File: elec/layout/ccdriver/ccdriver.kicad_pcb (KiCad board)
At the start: 2 copper layers, 40 x 40 mm, 0 parts

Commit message: readme
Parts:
- added C1: 25V 1uF X5R ±10% 0402 Multilayer Ceramic Capacitors MLCC - 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, lib:C0402, F.Cu at (172.7, 118.1)
- added C2: 25V 1uF X5R ±10% 0402 Multilayer Ceramic Capacitors MLCC - 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, lib:C0402, F.Cu at (169.2, 118.1)
- added C3: 16V 4.7uF X5R ±10% 0603 Multilayer Ceramic Capacitors MLCC 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, lib:C0603, F.Cu at (177.4, 117.1)
- added C4: 50V 1uF X5R ±10% 0603 Multilayer Ceramic Capacitors MLCC - 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, lib:C0603, F.Cu at (177.4, 112.6)
- added R1: 62.5mW Thick Film Resistors 50V ±100ppm/℃ ±1% 576Ω 0402 Chi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, lib:R0402, F.Cu at (169.2, 120.0)
- added R2: 62.5mW Thick Film Resistors 50V ±100ppm/℃ ±1% 4.7kΩ 0402 Ch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, lib:R0402, F.Cu at (215.3, 104.7)
- added R3: 62.5mW Thick Film Resistors 50V ±100ppm/℃ ±1% 4.7kΩ 0402 Ch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, lib:R0402, F.Cu at (218.3, 104.6)
- added R4: 62.5mW Thick Film Resistors 50V ±1% 300mΩ 0402 Chip Resisto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, lib:R0402, F.Cu at (182.9, 112.3)
- added U1: ?, lib:WSON-10_L2.0-W2.0-P0.40-BL-EP, F.Cu at (171.0, 118.8)
- added U2: ?, lib:SC-70-5_L2.1-W1.3-P0.65-LS2.1-BR, F.Cu at (182.9, 115.8)
- added U3: ?, lib:USB-C-SMD_KH-TYPE-C-16P, F.Cu at (216.5, 109.2)
- added U4: ?, lib:IND-SMD_L4.5-W4.0, F.Cu at (185.8, 103.3)
- added U5: ?, lib:SOD-923_L0.8-W0.6-LS1.0-RD-1, F.Cu at (176.6, 121.3)
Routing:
- net bms.ic-vcc: track 0.00 -> 6.47 mm, vias 0 -> 2
- net gnd: track 0.00 -> 4.50 mm
- net iset: track 0.00 -> 2.76 mm
- net cc2: track 0.00 -> 1.65 mm
- net cc1: track 0.00 -> 1.60 mm
- net vcc-1: track 0.00 -> 1.16 mm
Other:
- board outline removed

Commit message: edited cc driver
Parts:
- moved U3 45.0 mm to (173.1, 121.0), turned to -90 degrees
- moved R3 44.5 mm to (177.6, 122.8), turned to 0 degrees
- moved R2 40.6 mm to (177.6, 119.8), turned to 0 degrees
- moved L1 17.2 mm to (182.9, 120.3)
- moved R1 13.1 mm to (180.2, 112.7), turned to -90 degrees
- moved C4 11.7 mm to (187.0, 119.2), turned to -90 degrees
- moved C2 11.5 mm to (180.2, 114.6), turned to 90 degrees
- moved D1 10.4 mm to (186.0, 117.0), turned to 180 degrees
- moved U1 8.95 mm to (178.4, 113.9), turned to 180 degrees
- moved C1 5.34 mm to (176.7, 114.6), turned to 90 degrees
- moved R4 2.72 mm to (185.0, 114.0)
- moved C3 2.16 mm to (179.5, 116.5), turned to 180 degrees
- renumbered U5 to D1, U4 to L1
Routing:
- net bms.ic-vcc: track 6.47 -> 17.7 mm
- net sw: track 0.00 -> 5.02 mm
- net vcc-1: track 1.16 -> 4.17 mm
- net vcc: track 0.00 -> 1.65 mm
- net fb: track 0.00 -> 1.40 mm

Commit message: ccdriver
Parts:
- added C1: 25V 100nF X5R ±10% 0201 Multilayer Ceramic Capacitors MLCC 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, lib:C0201, F.Cu at (188.8, 116.5)
- added C6: 25V 10uF X5R ±10% 0805 Multilayer Ceramic Capacitors MLCC -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, lib:C0805, F.Cu at (172.4, 114.2)
- added R1: 50mW Thick Film Resistors ±5% 510Ω 0201 Chip Resistor - Sur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, lib:R0201, F.Cu at (191.0, 113.5)
- added U1: ?, lib:QFN-20_L3.0-W3.0-P0.40-TL-EP1.7, F.Cu at (191.8, 116.2)
- added U5: ?, lib:KEY-SMD_4P-L4.2-W3.2-P2.20-LS4.6, F.Cu at (191.8, 121.0)
- moved R4 0.60 mm to (178.0, 122.3)
- moved U4 0.60 mm to (173.5, 120.6)
- moved R3 0.60 mm to (178.0, 119.3)
- moved C4 0.25 mm to (179.5, 116.8)
- renumbered C1 to C2, C2 to C3, C3 to C4, C4 to C5, R1 to R2, R2 to R3, R3 to R4, R4 to R5, U1 to U2, U2 to U3, U3 to U4
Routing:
- net vcc-1: track 4.17 -> 13.4 mm, vias 0 -> 1
- net uc.ic-gnd: track 0.00 -> 6.97 mm, vias 0 -> 1
- net vcc: track 1.65 -> 8.25 mm, vias 0 -> 1
- net uc.ic-vcc: track 0.00 -> 4.26 mm
- net bms.ic-vcc: track 17.7 -> 19.3 mm
- net pa0_reset_updi: track 0.00 -> 1.21 mm, vias 0 -> 1
- net updi: track 0.00 -> 1.17 mm
- net nc: vias 0 -> 2
- net gnd: vias 0 -> 5
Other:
- board text added: "gnd"
- board text added: "updi"
- board text added: "vcc"

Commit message: ccdriver updates
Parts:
- added C7: 16V 4.7uF X5R ±10% 0603 Multilayer Ceramic Capacitors MLCC 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, lib:C0603, F.Cu at (187.8, 120.5)
- added CHG: ?, lib:LED0603-RD, F.Cu at (192.5, 122.8)
- added FULL: ?, lib:LED0603-RD, F.Cu at (192.5, 121.0)
- added R5: 62.5mW Thick Film Resistors 50V ±100ppm/℃ ±1% 220Ω 0402 Chi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, lib:R0402, F.Cu at (190.0, 121.0)
- added R6: 62.5mW Thick Film Resistors 50V ±1% ±200ppm/℃ 100Ω 0402 Chi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, lib:R0402, F.Cu at (189.8, 122.8)
- moved U5 20.1 mm to (173.2, 113.4)
- moved C6 11.8 mm to (178.8, 124.2), turned to 0 degrees
- moved C5 0.91 mm to (187.8, 118.8), turned to 0 degrees
- moved R3 0.26 mm to (178.0, 119.6)
- renumbered R5 to R7
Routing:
- net bms.ic-vcc: track 19.3 -> 21.6 mm
- net charge_led.resistor-cathode: track 0.00 -> 1.91 mm
- net full_led.resistor-cathode: track 0.00 -> 1.46 mm
- net gnd: track 4.50 -> 5.43 mm
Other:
- board outline added: 25.2 x 14.8 mm

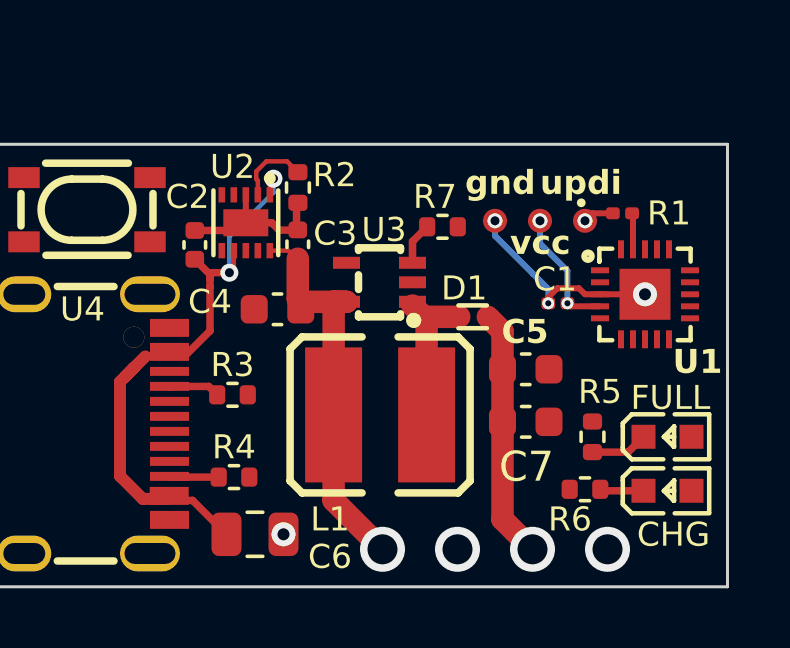
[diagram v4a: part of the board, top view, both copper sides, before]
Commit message: added 3v reg + layout edits
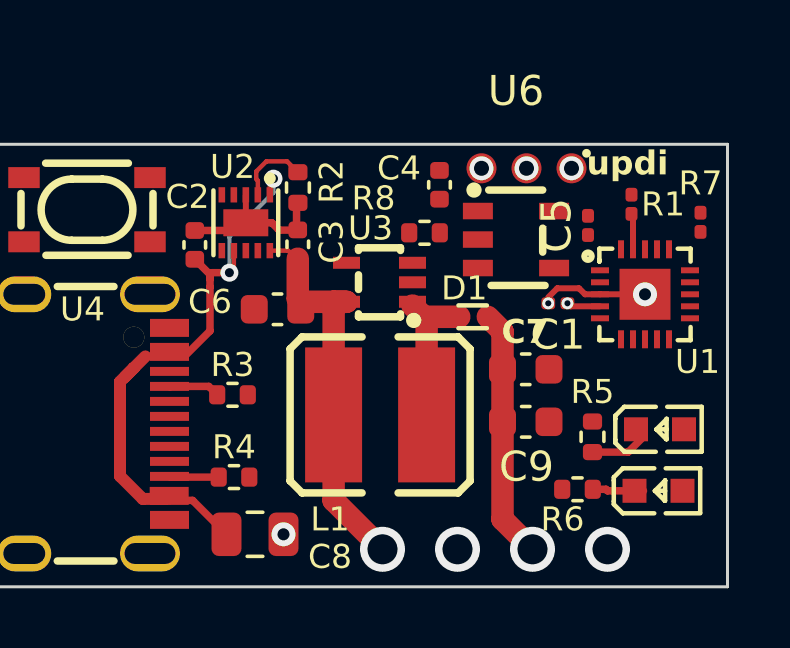
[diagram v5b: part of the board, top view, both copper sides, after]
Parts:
- added C4: 25V 1uF X5R ±10% 0402 Multilayer Ceramic Capacitors MLCC - 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, lib:C0402, F.Cu at (184.9, 112.6)
- added C5: 10V 1uF X5R ±20% 0201 Multilayer Ceramic Capacitors MLCC - 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, lib:C0201, F.Cu at (189.8, 114.0)
- added R7: 50mW Thick Film Resistors 25V ±1% ±200ppm/℃ 510kΩ 0201 Chip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, lib:R0201, F.Cu at (193.6, 113.8)
- added U6: ?, lib:SOT-23-5_L3.0-W1.7-P0.95-LS2.8-TL, F.Cu at (187.4, 114.4)
- moved R8 0.63 mm to (184.4, 114.2)
- moved R1 0.42 mm to (191.3, 113.2), turned to -90 degrees
- moved LED1 0.35 mm to (192.2, 120.8)
- moved LED2 0.30 mm to (192.2, 122.8)
- moved R6 0.25 mm to (189.5, 122.8)
- renumbered C4 to C6, C5 to C7, C6 to C8, C7 to C9, FULL to LED1, CHG to LED2, R7 to R8
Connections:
- C2 pad 2: gnd -> uc.ic-gnd
- C3 pad 2: gnd -> uc.ic-gnd
- C6 pad 2: gnd -> uc.ic-gnd
- C7 pad 2: gnd -> uc.ic-gnd
- C8 pad 2: gnd -> uc.ic-gnd
- C9 pad 2: gnd -> uc.ic-gnd
- R2 pad 2: gnd -> uc.ic-gnd
- R3 pad 2: gnd -> uc.ic-gnd
- R4 pad 2: gnd -> uc.ic-gnd
- R8 pad 2: gnd -> uc.ic-gnd
- U2 pad 11: gnd -> uc.ic-gnd
- U2 pad 3: gnd -> uc.ic-gnd
- U4 pad 1: gnd -> uc.ic-gnd
- U4 pad 2: gnd -> uc.ic-gnd
- U4 pad 3: gnd -> uc.ic-gnd
- U4 pad 4: gnd -> uc.ic-gnd
- U4 pad A1: gnd -> uc.ic-gnd
- U4 pad A12: gnd -> uc.ic-gnd
- U4 pad B1: gnd -> uc.ic-gnd
- U4 pad B12: gnd -> uc.ic-gnd
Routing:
- net gnd: track 5.43 -> 0.00 mm, vias 5 -> 0
- net uc.ic-vcc: track 4.26 -> 1.13 mm
- net uc.ic-gnd: track 6.97 -> 8.92 mm, vias 1 -> 6
- net fb: track 1.40 -> 0.00 mm
- net updi: track 1.17 -> 0.14 mm, vias 0 -> 1
- net vcc: vias 1 -> 2
- net pa0_reset_updi: vias 1 -> 0
- net nc: vias 2 -> 1
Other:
- board text removed: "gnd"
- board text removed: "vcc"

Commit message: ccdriver
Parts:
- added R9: 50mW Thick Film Resistors 25V ±1% ±200ppm/℃ 10kΩ 0201 Chip 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, lib:R0201, F.Cu at (189.4, 118.2)
- R8: value 62.5mW Thick Film Resistors 50V ±1% 300mΩ 0402 Chip Resistor - Surface Mount ROHS -> 100mW 300mΩ Chip Splitter 0ppm/℃~+300ppm/℃ ±1% 0201 Current Sense Resistors / Shunt Resistors ROHS; footprint lib:R0402 -> lib:R0201
- moved R5 1.10 mm to (189.2, 121.8), turned to 180 degrees
- moved L1 0.49 mm to (182.4, 120.3)
- moved C1 0.33 mm to (188.5, 116.6)
- moved C7 0.33 mm to (187.4, 118.8)
- moved U1 0.33 mm to (191.4, 116.3)
- moved C9 0.32 mm to (187.5, 120.4)
- moved R6 0.26 mm to (189.2, 122.8)
- moved R1 0.18 mm to (191.2, 113.4)
- moved C5 0.06 mm to (189.9, 113.9), turned to -90 degrees
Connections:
- C1 pad 2: uc.ic-gnd -> gnd
- C2 pad 2: uc.ic-gnd -> gnd
- C3 pad 2: uc.ic-gnd -> gnd
- C4 pad 2: uc.ic-gnd -> gnd
- C5 pad 2: uc.ic-gnd -> gnd
- C6 pad 2: uc.ic-gnd -> gnd
- C7 pad 2: uc.ic-gnd -> gnd
- C8 pad 2: uc.ic-gnd -> gnd
- C9 pad 2: uc.ic-gnd -> gnd
- LED1 pad 2: charge_led-vcc -> uc.ic-vcc-1
- LED2 pad 2: full_led-vcc -> uc.ic-vcc-2
- R2 pad 2: uc.ic-gnd -> gnd
- R3 pad 2: uc.ic-gnd -> gnd
- R4 pad 2: uc.ic-gnd -> gnd
- R5 pad 2: charge_led-gnd -> gnd
- R6 pad 2: full_led-gnd -> gnd
- R8 pad 2: uc.ic-gnd -> gnd
- U1 pad 10: pb4 -> uc.ic-vcc-2
- U1 pad 21: uc.ic-gnd -> gnd
- U1 pad 3: uc.ic-gnd -> gnd
- U1 pad 6: pa5 -> in
- U1 pad 9: pb5 -> uc.ic-vcc-1
- U2 pad 11: uc.ic-gnd -> gnd
- U2 pad 3: uc.ic-gnd -> gnd
- U4 pad 1: uc.ic-gnd -> gnd
- U4 pad 2: uc.ic-gnd -> gnd
- U4 pad 3: uc.ic-gnd -> gnd
- U4 pad 4: uc.ic-gnd -> gnd
- U4 pad A1: uc.ic-gnd -> gnd
- U4 pad A12: uc.ic-gnd -> gnd
- U4 pad B1: uc.ic-gnd -> gnd
- U4 pad B12: uc.ic-gnd -> gnd
- U5 pad 3: out -> gnd
- U5 pad 4: out -> gnd
- U6 pad 2: uc.ic-gnd -> gnd
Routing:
- net uc.ic-gnd: track 8.92 -> 0.00 mm, vias 6 -> 0
- net gnd: track 0.00 -> 8.92 mm, vias 0 -> 7
- net uc.ic-vcc-2: track 0.00 -> 6.69 mm
- net uc.ic-vcc-1: track 0.00 -> 3.47 mm
- net updi: track 0.14 -> 2.75 mm
- net vcc: track 8.37 -> 9.84 mm
- net uc.ic-vcc: track 1.13 -> 2.36 mm, vias 0 -> 1
- net fb: track 0.00 -> 1.05 mm
- net charge_led.resistor-cathode: track 1.91 -> 2.43 mm
- net nc: vias 1 -> 0

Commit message: ccdriver
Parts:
- removed the R7 at (193.6, 113.8)
- C1: value 25V 100nF X5R ±10% 0201 Multilayer Ceramic Capacitors MLCC - SMD/SMT ROHS -> 10V 100nF X5R ±10% 0201 Multilayer Ceramic Capacitors MLCC - SMD/SMT ROHS
- R7: renamed from R8; value 100mW 300mΩ Chip Splitter 0ppm/℃~+300ppm/℃ ±1% 0201 Current Sense Resistors / Shunt Resistors ROHS -> 100mW 300mΩ Current Sensing Resistors ±50ppm/℃ ±1% 0201 Current Sense Resistors / Shunt Resistors ROHS
- renumbered R9 to R8
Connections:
- U1 pad 20: pa1 -> ctrl
- U3 pad 2: led_driver-gnd -> gnd
- U6 pad 3: en -> vcc-1
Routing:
- net gnd: track 8.92 -> 121.0 mm, vias 7 -> 11
- net in: track 0.00 -> 21.9 mm, vias 0 -> 2
- net vcc-1: track 13.4 -> 23.4 mm, vias 1 -> 3
- net ctrl: track 0.00 -> 9.15 mm, vias 0 -> 2
- net uc.ic-vcc: track 2.36 -> 11.3 mm, vias 1 -> 2
- net dm: track 0.00 -> 2.84 mm
- net dp: track 0.00 -> 2.84 mm
- net bms.ic-vcc: track 21.6 -> 22.7 mm
- net vcc: vias 2 -> 1

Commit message: cc driver planes
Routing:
- net gnd: vias 11 -> 15
- added copper zone on B.Cu, net gnd
- added copper zone on F.Cu, net gnd
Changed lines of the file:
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@@
 		(tags "resistor")
 		(property "Reference" "R5"
-			(at -1.79 0.15 0)
+			(at 1.74 -0.21 0)
 			(layer "F.SilkS")
 			(effects
@@
 	)
 	(via
+		(at 193.4 114)
+		(size 0.8)
+		(drill 0.4)
+		(layers "F.Cu" "B.Cu")
+		(net 39)
+	)
+	(via
 		(at 189.9 114.25)
 		(size 0.4)
@@
 	)
 	(via
+		(at 173.15 113.43)
+		(size 0.8)
+		(drill 0.4)
+		(layers "F.Cu" "B.Cu")
+		(net 39)
+	)
+	(via
 		(at 185.5 124.75)
 		(size 1.5)
@@
 		(net 39)
 	)
+	(via
+		(at 179 121)
+		(size 0.8)
+		(drill 0.4)
+		(layers "F.Cu" "B.Cu")
+		(net 39)
+	)
+	(via
+		(at 182.4 113)
+		(size 0.8)
+		(drill 0.4)
+		(layers "F.Cu" "B.Cu")
+		(net 39)
+	)
 	(segment
 		(start 172.5 124.89)
@@
 		(net 41)
 	)
+	(zone
+		(net 39)
+		(net_name "gnd")
+		(layers "F&B.Cu")
+		(hatch edge 0.5)
+		(connect_pads
+			(clearance 0.5)
+		)
+		(min_thickness 0.25)
+		(filled_areas_thickness no)
+		(fill yes
+			(thermal_gap 0.5)
+			(thermal_bridge_width 0.5)
+		)
+		(polygon
+			(pts
+				(xy 195 110.5) (xy 195 127) (xy 168.5 127) (xy 168.5 110.5)
+			)
+		)
+	)
 	(group "bms"
